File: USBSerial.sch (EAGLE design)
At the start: 27 parts, among them IC1 ATMEGA16U2 QFN-32, J1 Gnd, J2 DFU

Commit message: Changed CTS / RTS assignment
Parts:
- removed H1: M12PTH, freetronics-original:M12PTH
- added LED2, LED3, LED4: (no value), freetronics-jon:LED0603
- added R7, R8, R9: 1K 0603, freetronics:RESISTOR0603
- added U$23: M13, freetronics-jon:M13
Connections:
- removed net RTS: H4.6, IC1.(RTS)PD6
- new net N$3: LED2.C, R7.2
- new net N$7: LED4.C, R8.2
- new net N$9: LED3.C, R9.2
- new net PD6: IC1.(RTS)PD6, U$23.10
- net CTS: now also H4.6; no longer H4.2
- net PB0: now also U$23.9; no longer H1.9
- net PB4: now also U$23.8; no longer H1.8
- net PB5: now also U$23.7; no longer H1.7
- net PB6: now also U$23.6; no longer H1.6
- net PB7: now also U$23.5; no longer H1.5
- net PC2: now also U$23.13; no longer H1.12
- net PC4: now also U$23.1; no longer H1.1
- net PC5: now also U$23.2; no longer H1.2
- net PC6: now also U$23.3; no longer H1.3
- net PC7: now also U$23.4; no longer H1.4
- net PD0: now also U$23.12; no longer H1.11
- net PD1: now also U$23.11; no longer H1.10
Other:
- note added: "CTS (green)"
- note added: "NC (brown)"
- note added: "V1.1 (17-04-2013)"
- note removed: "CTS (brown)"
- note removed: "RTS (green)"
- note removed: "V1.0 (06-04-2013)"

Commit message: v1.1 release: Separate LEDs near TX/RX/VCC pins; PCB tab over connector; label improvements
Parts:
- removed LED4: (no value), freetronics-jon:LED0603
- removed R9: 1K 0603, freetronics:RESISTOR0603
- LED1: value RGB -> GREEN 0603; device freetronics-master-v1:RGBLEDSMT -> freetronics-jon:LED0603
- LED2: value (none) -> RED 0603
- LED3: value (none) -> BLUE 0603
- R4: value 1k -> 22R 0603; device freetronics-luke:CAY16 -> freetronics:RESISTOR0603
- R6: value 22R 0603 -> 1K 0603
- renumbered L2 to L1, U$23 to H1
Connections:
- removed net N$4: LED1.C-R, R4B.1
- removed net N$5: LED1.C-B, R4C.1
- removed net N$6: LED1.C-G, R4A.1
- removed net N$7 (its old number): LED4.C, R8.2
- new net N$3: LED1.C, R6.2
- net GND: now also R8.1; no longer R4C.2
- net N$16: now also R5.2; no longer R6.2
- net N$17: now also R4.2; no longer R5.2
- net N$9: now also R8.2; no longer R9.2
- net RD+: now also R5.1; no longer R6.1
- net RD-: now also R4.1; no longer R5.1
- net RXLED: now also R7.1; no longer R4B.2
- net TXLED: now also R6.1; no longer R4A.2
- net VDD: now also LED1.A, LED2.A, LED3.A; no longer LED1.A-B, LED1.A-G, LED1.A-R
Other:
- note removed: "R4: 1k SMD quad resistor pack"
- note removed: "Same as LeoStick."
- note removed: "Small SMD RGB."
- moved on the sheet: LED2, LED3, R5, R6, R7, R8

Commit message: Minor cleanups for v1.2 release
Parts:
- removed H5: VDD Select, freetronics-luke:JUMPER_SPDT
- added SW1: MK-12C02-PB, freetronics-jon:SWITCH-SPDT-4TABSSMT
- XTL1: device freetronics-master-v1:CRYSTALHC49US -> freetronics-jon:CRYSTALHC49UV
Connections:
- net +3V3: now also SW1.A; no longer H5.1
- net +5V: now also SW1.B; no longer H5.3
- net GND: now also SW1.MNT@1, SW1.MNT@2, SW1.MNT@3, SW1.MNT@4
- net VDD: now also SW1.COM; no longer H5.2
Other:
- note added: "3.3V Regulator"
- note added: "I/O Breakout"
- note added: "Output Voltage Selection"
- note added: "V1.2 (2013-05-06)"
- note removed: "I/O interface pin headers"
- note removed: "Jumper on 3 x 0.1" through-hole"
- note removed: "V1.1 (17-04-2013)"
- note removed: "header pins."
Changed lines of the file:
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@@
 <part name="C4" library="freetronics" deviceset="CAP" device="0603" value="1uF 0603"/>
 <part name="F1" library="freetronics-luke" deviceset="PTC" device="" value="500mA PTC 1812"/>
-<part name="XTL1" library="freetronics-master-v1" deviceset="CRYSTAL" device="HC49US" value="16MHz"/>
+<part name="XTL1" library="freetronics-jon" deviceset="CRYSTAL" device="HC49UV" value="16MHz"/>
 <part name="C3" library="freetronics" deviceset="CAP" device="0603" value="100n 0603"/>
 <part name="J1" library="freetronics-jon" deviceset="SJC" device="N" value="Gnd"/>
@@
 <part name="U$2" library="freetronics-luke" deviceset="VDD" device=""/>
 <part name="U$10" library="freetronics-luke" deviceset="VDD" device=""/>
-<part name="U$11" library="freetronics-luke" deviceset="+5V" device=""/>
-<part name="U$12" library="freetronics-luke" deviceset="+3.3V" device=""/>
-<part name="U$19" library="freetronics-luke" deviceset="VDD" device=""/>
 <part name="C5" library="freetronics" deviceset="CAP" device="0603" value="100n 0603"/>
 <part name="U$20" library="freetronics-luke" deviceset="GND" device=""/>
@@
 <part name="H3" library="freetronics-luke" deviceset="HEADER_2X3" device="" value="ICSP"/>
 <part name="REG1" library="freetronics-luke" deviceset="LD1117-FIXED" device="" value="LD1117-33 SOT-223"/>
-<part name="H5" library="freetronics-luke" deviceset="JUMPER_SPDT" device="" value="VDD Select"/>
 <part name="H2" library="freetronics-jon" deviceset="USB-6P" device="SMT"/>
 <part name="Z1" library="freetronics" deviceset="RESISTOR" device="0603" value="PGB1010603"/>
@@
 <part name="R8" library="freetronics" deviceset="RESISTOR" device="0603" value="1K 0603"/>
 <part name="U$18" library="freetronics-luke" deviceset="GND" device=""/>
+<part name="SW1" library="freetronics-jon" deviceset="SWITCH-SPDT-4TABS" device="SMT" value="MK-12C02-PB"/>
+<part name="U$24" library="freetronics-luke" deviceset="GND" device=""/>
+<part name="U$25" library="freetronics-luke" deviceset="VDD" device=""/>
+<part name="U$26" library="freetronics-luke" deviceset="+3.3V" device=""/>
+<part name="U$27" library="freetronics-luke" deviceset="+5V" device=""/>
 </parts>
 <sheets>
@@
 <text x="63.5" y="109.22" size="1.27" layer="98">HC49US</text>
 <text x="7.62" y="20.32" size="3.048" layer="94">Freetronics USB-Serial Adapter</text>
-<text x="33.02" y="14.478" size="1.778" layer="94">V1.1 (17-04-2013)</text>
+<text x="33.02" y="14.478" size="1.778" layer="94">V1.2 (2013-05-06)</text>
 <text x="7.62" y="14.478" size="1.778" layer="94">SKU: USBSERIAL</text>
 <text x="7.366" y="9.398" size="1.778" layer="94">(C)2013 Freetronics Pty Ltd: www.freetronics.com</text>
 <text x="7.366" y="6.35" size="1.778" layer="94">Licensed under the TAPR Open Hardware License: www.tapr.org/ohl</text>
 <text x="63.246" y="14.478" size="1.778" layer="94">www.freetronics.com/usbserial</text>
-<text x="205.74" y="33.02" size="1.27" layer="98">Jumper on 3 x 0.1" through-hole</text>
-<text x="205.74" y="30.48" size="1.27" layer="98">header pins.</text>
-<text x="20.32" y="127" size="1.27" layer="98">I/O interface pin headers</text>
 <frame x1="0" y1="0" x2="248.92" y2="185.42" columns="8" rows="5" layer="94"/>
 <frame x1="5.08" y1="12.7" x2="109.22" y2="25.4" columns="0" rows="0" layer="94" border-left="no" border-top="no" border-right="no" border-bottom="no"/>
@@
 <text x="213.36" y="71.12" size="1.778" layer="97">NC (brown)</text>
 <text x="213.36" y="68.58" size="1.778" layer="97">GND (black)</text>
+<text x="182.88" y="43.18" size="1.778" layer="97">Output Voltage Selection</text>
+<text x="127" y="43.18" size="1.778" layer="97">3.3V Regulator</text>
+<text x="20.32" y="172.72" size="1.778" layer="97">I/O Breakout</text>
 </plain>
 <instances>
@@
 <attribute name="VALUE" x="200.66" y="119.38" size="1.27" layer="96"/>
 </instance>
-<instance part="U$11" gate="G$1" x="205.74" y="22.86" smashed="yes" rot="R270">
-<attribute name="VALUE" x="205.74" y="25.4" size="1.27" layer="96"/>
-</instance>
-<instance part="U$12" gate="G$1" x="190.5" y="22.86" smashed="yes" rot="R90">
-<attribute name="VALUE" x="185.42" y="20.32" size="1.27" layer="96"/>
-</instance>
-<instance part="U$19" gate="G$1" x="205.74" y="15.24" smashed="yes" rot="R270">
-<attribute name="VALUE" x="205.74" y="17.78" size="1.27" layer="96"/>
-</instance>
 <instance part="C5" gate="G$1" x="132.08" y="22.86" smashed="yes">
 <attribute name="NAME" x="127" y="25.4" size="1.27" layer="95"/>
@@
 <attribute name="NAME" x="137.16" y="35.56" size="1.27" layer="95"/>
 <attribute name="VALUE" x="137.16" y="33.528" size="1.27" layer="96"/>
-</instance>
-<instance part="H5" gate="G$1" x="198.12" y="30.48" smashed="yes">
-<attribute name="NAME" x="193.04" y="35.56" size="1.27" layer="95"/>
-<attribute name="VALUE" x="193.04" y="33.02" size="1.27" layer="96"/>
 </instance>
 <instance part="H2" gate="G$1" x="30.48" y="83.82" rot="R180"/>
@@
 </instance>
 <instance part="U$18" gate="G$1" x="175.26" y="124.46"/>
+<instance part="SW1" gate="G$1" x="198.12" y="27.94" smashed="yes">
+<attribute name="VALUE" x="191.135" y="34.67" size="1.778" layer="96"/>
+<attribute name="PART" x="196.215" y="37.21" size="1.778" layer="95"/>
+</instance>
+<instance part="U$24" gate="G$1" x="190.5" y="15.24"/>
+<instance part="U$25" gate="G$1" x="187.96" y="33.02" smashed="yes">
+<attribute name="VALUE" x="185.42" y="33.02" size="1.27" layer="96" rot="R90"/>
+</instance>
+<instance part="U$26" gate="G$1" x="213.36" y="33.02" smashed="yes">
+<attribute name="VALUE" x="210.82" y="38.1" size="1.27" layer="96" rot="R270"/>
+</instance>
+<instance part="U$27" gate="G$1" x="220.98" y="33.02" smashed="yes">
+<attribute name="VALUE" x="218.44" y="33.02" size="1.27" layer="96" rot="R90"/>
+</instance>
 </instances>
 <busses>
@@
 <pinref part="U$18" gate="G$1" pin="GND"/>
 <wire x1="175.26" y1="127" x2="175.26" y2="129.54" width="0.1524" layer="91"/>
+</segment>
+<segment>
+<pinref part="SW1" gate="G$1" pin="MNT@1"/>
+<pinref part="U$24" gate="G$1" pin="GND"/>
+<wire x1="193.04" y1="22.86" x2="190.5" y2="22.86" width="0.1524" layer="91"/>
+<wire x1="190.5" y1="22.86" x2="190.5" y2="20.32" width="0.1524" layer="91"/>
+<pinref part="SW1" gate="G$1" pin="MNT@2"/>
+<wire x1="190.5" y1="20.32" x2="190.5" y2="17.78" width="0.1524" layer="91"/>
+<wire x1="193.04" y1="20.32" x2="190.5" y2="20.32" width="0.1524" layer="91"/>
+<pinref part="SW1" gate="G$1" pin="MNT@3"/>
+<wire x1="203.2" y1="22.86" x2="205.74" y2="22.86" width="0.1524" layer="91"/>
+<wire x1="205.74" y1="22.86" x2="205.74" y2="20.32" width="0.1524" layer="91"/>
+<wire x1="205.74" y1="20.32" x2="205.74" y2="17.78" width="0.1524" layer="91"/>
+<wire x1="205.74" y1="17.78" x2="190.5" y2="17.78" width="0.1524" layer="91"/>
+<pinref part="SW1" gate="G$1" pin="MNT@4"/>
+<wire x1="203.2" y1="20.32" x2="205.74" y2="20.32" width="0.1524" layer="91"/>
+<junction x="190.5" y="17.78"/>
+<junction x="190.5" y="20.32"/>
+<junction x="205.74" y="20.32"/>
 </segment>
 </net>
@@
 </segment>
 <segment>
-<wire x1="200.66" y1="25.4" x2="200.66" y2="22.86" width="0.1524" layer="91"/>
-<wire x1="200.66" y1="22.86" x2="203.2" y2="22.86" width="0.1524" layer="91"/>
-<pinref part="U$11" gate="G$1" pin="+5V"/>
-<pinref part="H5" gate="G$1" pin="3"/>
+<pinref part="SW1" gate="G$1" pin="B"/>
+<pinref part="U$27" gate="G$1" pin="+5V"/>
+<wire x1="203.2" y1="25.4" x2="220.98" y2="25.4" width="0.1524" layer="91"/>
+<wire x1="220.98" y1="25.4" x2="220.98" y2="30.48" width="0.1524" layer="91"/>
 </segment>
 </net>
@@
 </segment>
 <segment>
-<wire x1="195.58" y1="25.4" x2="195.58" y2="22.86" width="0.1524" layer="91"/>
-<wire x1="195.58" y1="22.86" x2="193.04" y2="22.86" width="0.1524" layer="91"/>
-<pinref part="U$12" gate="G$1" pin="+3V3"/>
-<pinref part="H5" gate="G$1" pin="1"/>
+<pinref part="SW1" gate="G$1" pin="A"/>
+<pinref part="U$26" gate="G$1" pin="+3V3"/>
+<wire x1="203.2" y1="30.48" x2="213.36" y2="30.48" width="0.1524" layer="91"/>
 </segment>
 </net>
@@
 </segment>
 <segment>
-<wire x1="198.12" y1="25.4" x2="198.12" y2="15.24" width="0.1524" layer="91"/>
-<wire x1="198.12" y1="15.24" x2="203.2" y2="15.24" width="0.1524" layer="91"/>
-<pinref part="U$19" gate="G$1" pin="VDD"/>
-<pinref part="H5" gate="G$1" pin="2"/>
-</segment>
-<segment>
 <wire x1="200.66" y1="73.66" x2="198.12" y2="73.66" width="0.1524" layer="91"/>
 <wire x1="198.12" y1="83.82" x2="198.12" y2="73.66" width="0.1524" layer="91"/>
@@
 <pinref part="U$22" gate="G$1" pin="VDD"/>
 </segment>
-</net>
+<segment>
+<pinref part="SW1" gate="G$1" pin="COM"/>
+<pinref part="U$25" gate="G$1" pin="VDD"/>
+<wire x1="193.04" y1="27.94" x2="187.96" y2="27.94" width="0.1524" layer="91"/>
+<wire x1="187.96" y1="27.94" x2="187.96" y2="30.48" width="0.1524" layer="91"/>
+</segment>
+</net>

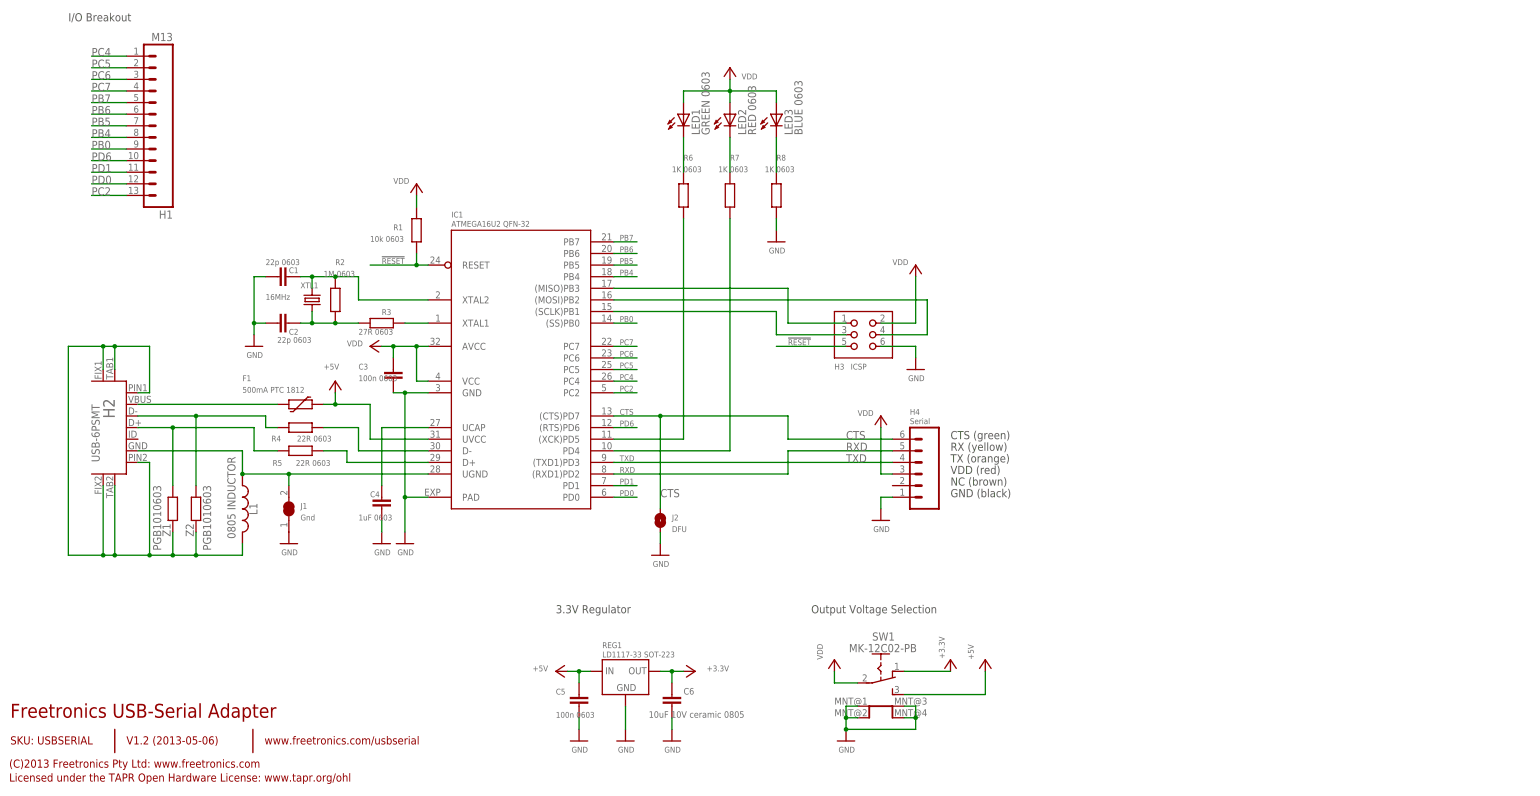
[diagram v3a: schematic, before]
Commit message: Replaced USB connector with USB-C
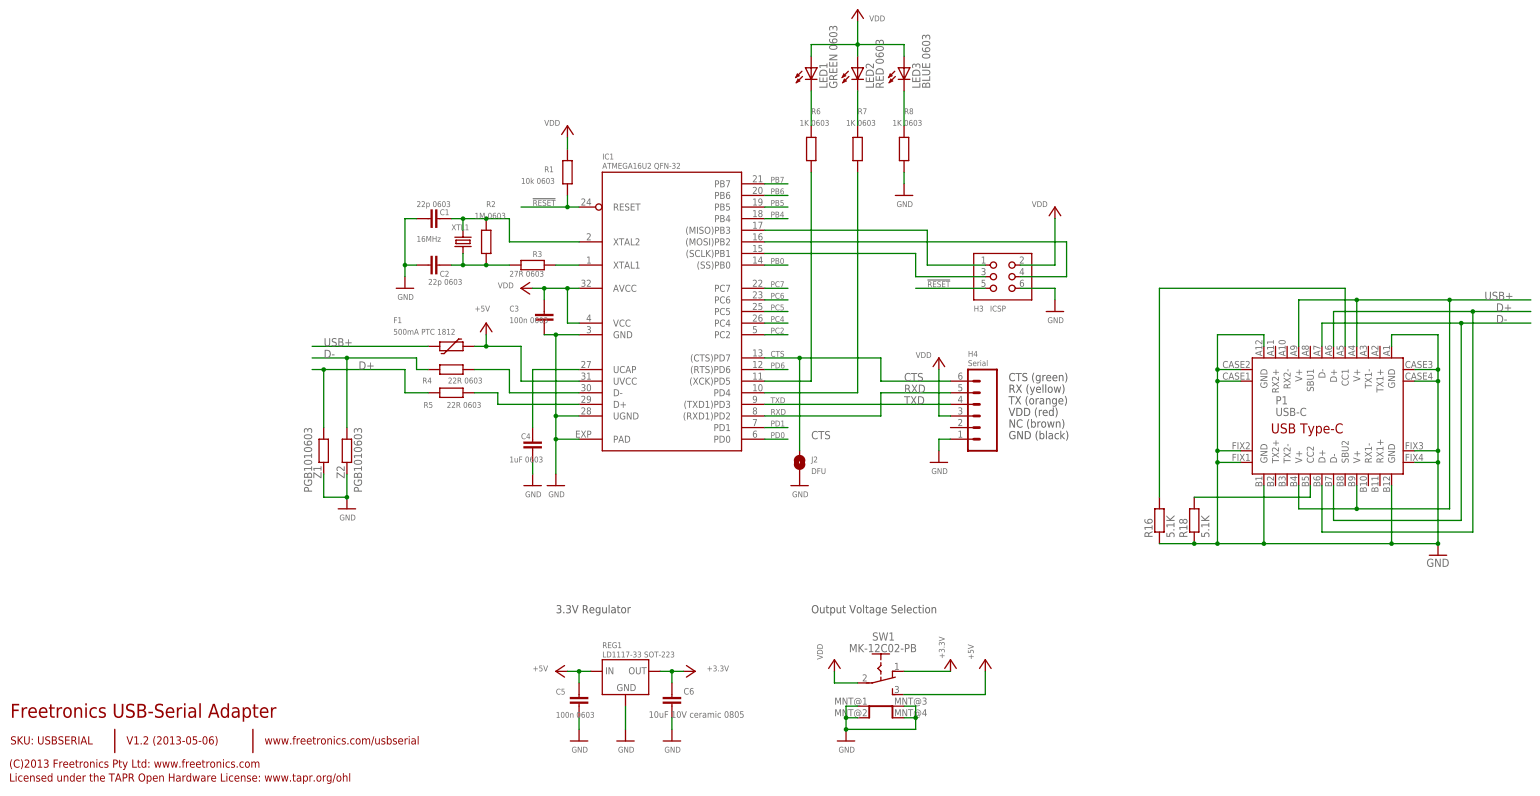
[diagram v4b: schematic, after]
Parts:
- removed H1: M13, freetronics-jon:M13
- removed H2: USB-6PSMT, freetronics-jon:USB-6PSMT
- removed J1: Gnd, freetronics-jon:SJCN
- removed L1: 0805 INDUCTOR, freetronics-master-v1:INDUCTOR0805-LARGE
- added P1: USB-C, freetronics-jon:USB-C
- added R16, R18: 5.1K, freetronics-original:RESISTOR0603
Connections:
- removed net N$1: H2.GND, IC1.UGND, J1.2, L1.1
- removed net N$115: F1.P$1, H2.VBUS
- removed net N$16: H2.D+, R5.2, Z1.1
- removed net N$17: H2.D-, R4.2, Z2.1
- removed net N$8: H2.FIX1, H2.FIX2, H2.PIN1, H2.PIN2, H2.TAB1, H2.TAB2, L1.2, Z1.2, Z2.2
- new net D+: P1.D+@A6, P1.D+@B6, R5.2, Z1.1
- new net D-: P1.D-@A7, P1.D-@B7, R4.2, Z2.1
- new net N$4: P1.CC1, R16.2
- new net N$5: P1.CC2, R18.2
- new net USB+: F1.P$1, P1.V+@A4, P1.V+@A9, P1.V+@B4, P1.V+@B9
- net GND: now also IC1.UGND, P1.GND@A1, P1.GND@A12, P1.GND@B1, P1.GND@B12, P1.GND@CASE1, P1.GND@CASE2, P1.GND@CASE3, P1.GND@CASE4, P1.GND@FIX1, P1.GND@FIX2, P1.GND@FIX3, P1.GND@FIX4, R16.1, R18.1, Z1.2, Z2.2; no longer J1.1
- net PB0: no longer H1.9
- net PB4: no longer H1.8
- net PB5: no longer H1.7
- net PB6: no longer H1.6
- net PB7: no longer H1.5
- net PC2: no longer H1.13
- net PC4: no longer H1.1
- net PC5: no longer H1.2
- net PC6: no longer H1.3
- net PC7: no longer H1.4
- net PD0: no longer H1.12
- net PD1: no longer H1.11
- net PD6: no longer H1.10
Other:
- note removed: "I/O Breakout"
- moved on the sheet: C1, C2, C3, C4, F1, H3, H4, IC1, J2, LED1, LED2, LED3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
